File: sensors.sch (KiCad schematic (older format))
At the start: 13 parts, among them U2001 VCNL4040, U2002 LSM9DS1, U2003 74LVC1G332

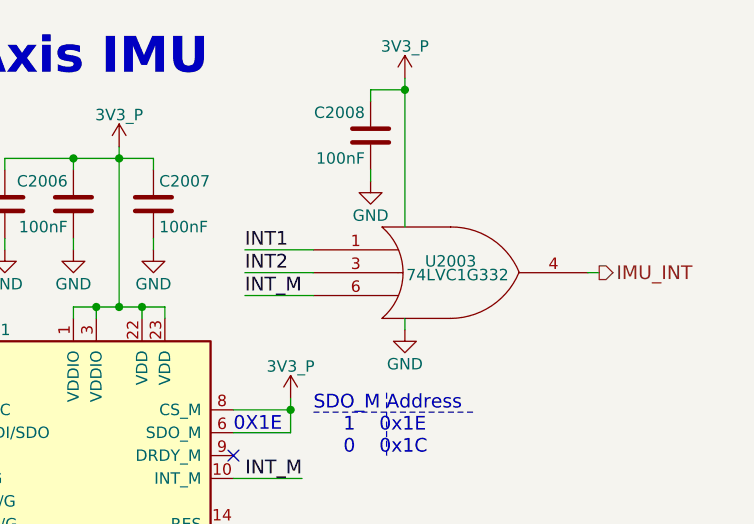
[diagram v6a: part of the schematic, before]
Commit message: Add camera/CSI circuit, include second switch that is part of the audio+camera DPDT for killing both simultaneously, level shifters used for camera's I/O that requires it, footprints for a 1.8V LDO which may be used by DVDD will be included
External DVDD (1.8V LDO) needs to be tested if it's needed (datasheet says an internal DVDD can be used, as is the case with Boundary Devices' OV5640 camera).
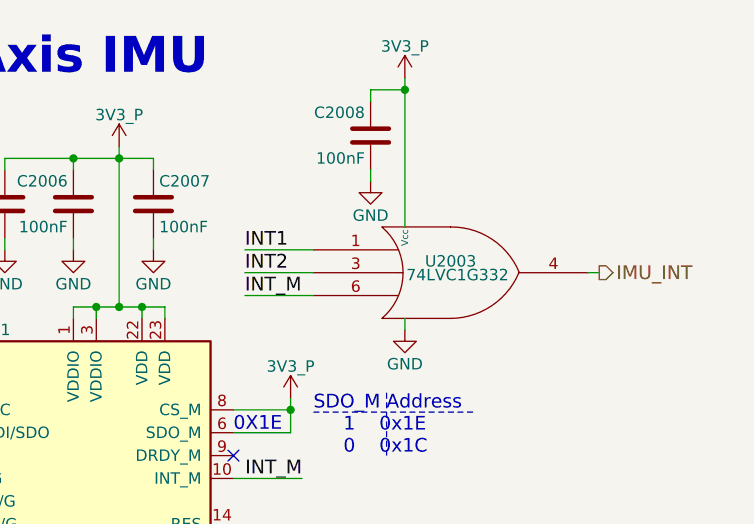
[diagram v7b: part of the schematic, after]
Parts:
- removed U2003: 74LVC1G332, http://www.ti.com/lit/ds/symlink/sn74lvc1g332.pdf, symbol SN74LVC1G332
- added U2003: 74LVC1G332, symbol 74LVC1G332
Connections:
- net 3V3_P: now also U2003.5 (Vcc)
- net GND: now also U2003.2 (GND)
- net IMU_INT: now also U2003.4
- net INT1: now also U2003.1
- net INT2: now also U2003.3
- net INT_M: now also U2003.6
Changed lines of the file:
@@
 $EndComp
 $Comp
-L GND #PWR2005
+L GND #PWR0341
 U 1 1 5B067AE0
 P 4550 3450
-F 0 "#PWR2005" H 4550 3200 50  0001 C CNN
+F 0 "#PWR0341" H 4550 3200 50  0001 C CNN
 F 1 "GND" H 4550 3300 50  0000 C CNN
 F 2 "" H 4550 3450 50  0001 C CNN
@@
 $EndComp
 $Comp
-L GND #PWR2003
+L GND #PWR0342
 U 1 1 5B068781
 P 3800 4100
-F 0 "#PWR2003" H 3800 3850 50  0001 C CNN
+F 0 "#PWR0342" H 3800 3850 50  0001 C CNN
 F 1 "GND" H 3800 3950 50  0000 C CNN
 F 2 "" H 3800 4100 50  0001 C CNN
@@
 $EndComp
 $Comp
-L GND #PWR2002
+L GND #PWR0343
 U 1 1 5B068863
 P 3600 2650
-F 0 "#PWR2002" H 3600 2400 50  0001 C CNN
+F 0 "#PWR0343" H 3600 2400 50  0001 C CNN
 F 1 "GND" H 3600 2500 50  0000 C CNN
 F 2 "" H 3600 2650 50  0001 C CNN
@@
 $EndComp
 $Comp
-L 3V3_P #PWR2004
+L 3V3_P #PWR0344
 U 1 1 5B0689D2
 P 4550 2200
-F 0 "#PWR2004" H 4550 2050 50  0001 C CNN
+F 0 "#PWR0344" H 4550 2050 50  0001 C CNN
 F 1 "3V3_P" H 4550 2350 50  0000 C CNN
 F 2 "" H 4550 2200 50  0001 C CNN
@@
 $EndComp
 $Comp
-L 3V3_P #PWR2001
+L 3V3_P #PWR0345
 U 1 1 5B069B9B
 P 2600 3150
-F 0 "#PWR2001" H 2600 3000 50  0001 C CNN
+F 0 "#PWR0345" H 2600 3000 50  0001 C CNN
 F 1 "3V3_P" H 2600 3290 50  0000 C CNN
 F 2 "" H 2600 3150 50  0001 C CNN
@@
 $EndComp
 $Comp
-L PWR_FLAG #FLG2001
+L PWR_FLAG #FLG0346
 U 1 1 5B13CB3F
 P 3800 2200
-F 0 "#FLG2001" H 3800 2275 50  0001 C CNN
+F 0 "#FLG0346" H 3800 2275 50  0001 C CNN
 F 1 "PWR_FLAG" H 3800 2350 50  0000 C CNN
 F 2 "" H 3800 2200 50  0001 C CNN
@@
 $EndComp
 $Comp
-L GND #PWR2008
+L GND #PWR0347
 U 1 1 5B15906B
 P 8200 4450
-F 0 "#PWR2008" H 8200 4200 50  0001 C CNN
+F 0 "#PWR0347" H 8200 4200 50  0001 C CNN
 F 1 "GND" H 8200 4300 50  0000 C CNN
 F 2 "" H 8200 4450 50  0001 C CNN
@@
 $EndComp
 $Comp
-L 3V3_P #PWR2010
+L 3V3_P #PWR0348
 U 1 1 5B15B71F
 P 8500 1800
-F 0 "#PWR2010" H 8500 1650 50  0001 C CNN
+F 0 "#PWR0348" H 8500 1650 50  0001 C CNN
 F 1 "3V3_P" H 8500 1940 50  0000 C CNN
 F 2 "" H 8500 1800 50  0001 C CNN
@@
 $EndComp
 $Comp
-L GND #PWR2011
+L GND #PWR0349
 U 1 1 5B15B942
 P 8650 2250
-F 0 "#PWR2011" H 8650 2000 50  0001 C CNN
+F 0 "#PWR0349" H 8650 2000 50  0001 C CNN
 F 1 "GND" H 8650 2100 50  0000 C CNN
 F 2 "" H 8650 2250 50  0001 C CNN
@@
 $EndComp
 $Comp
-L GND #PWR2009
+L GND #PWR0350
 U 1 1 5B15B987
 P 8300 2250
-F 0 "#PWR2009" H 8300 2000 50  0001 C CNN
+F 0 "#PWR0350" H 8300 2000 50  0001 C CNN
 F 1 "GND" H 8300 2100 50  0000 C CNN
 F 2 "" H 8300 2250 50  0001 C CNN
@@
 $EndComp
 $Comp
-L GND #PWR2007
+L GND #PWR0351
 U 1 1 5B15BC52
 P 8000 2250
-F 0 "#PWR2007" H 8000 2000 50  0001 C CNN
+F 0 "#PWR0351" H 8000 2000 50  0001 C CNN
 F 1 "GND" H 8000 2100 50  0000 C CNN
 F 2 "" H 8000 2250 50  0001 C CNN
@@
 	-1   0    0    -1
 $EndComp
-$Comp
-L SN74LVC1G332 U2003
-U 1 1 5B168FC1
-P 9950 2350
-F 0 "U2003" H 9950 2400 50  0000 C CNN
-F 1 "74LVC1G332" H 9980 2340 50  0000 C CNN
-F 2 "http://www.ti.com/lit/ds/symlink/sn74lvc1g332.pdf" H 9950 2350 50  0001 C CNN
-F 3 "" H 9950 2350 50  0001 C CNN
-F 4 "Texas Instruments" H 9950 2350 60  0001 C CNN "MFG Name"
-F 5 "SN74LVC1G332DCKR" H 9950 2350 60  0001 C CNN "MFG Part Num"
-F 6 "SN74LVC1G332DCKR" H 9950 2350 60  0001 C CNN "Distrib PN"
-F 7 "https://store.ti.com/SN74LVC1G332DCKR.aspx?HQS=corp-tistore-null-storeinv-invf-store-octopart-wwe" H 9950 2350 60  0001 C CNN "Distrib Link"
-F 8 "-" H 9950 2350 60  0001 C CNN "Tolerance"
-F 9 "https://www.digikey.com/products/en/integrated-circuits-ics/logic-gates-and-inverters/705?FV=ffe002c1&quantity=&ColumnSort=1000011&page=1&k=1G332&pageSize=500" H 9950 2350 60  0001 C CNN "Others"
-	1    9950 2350
-	1    0    0    -1
-$EndComp
 Text Label 9050 2450 0    60   ~ 0
 INT_M
@@
 INT_M
 $Comp
-L 3V3_P #PWR2006
+L 3V3_P #PWR0352
 U 1 1 5B176622
 P 6900 3200
-F 0 "#PWR2006" H 6900 3050 50  0001 C CNN
+F 0 "#PWR0352" H 6900 3050 50  0001 C CNN
 F 1 "3V3_P" H 6900 3340 50  0000 C CNN
 F 2 "" H 6900 3200 50  0001 C CNN
@@
 $EndComp
 $Comp
-L 3V3_P #PWR2012
+L 3V3_P #PWR0353
 U 1 1 5B1766DE
 P 9250 2900
-F 0 "#PWR2012" H 9250 2750 50  0001 C CNN
+F 0 "#PWR0353" H 9250 2750 50  0001 C CNN
 F 1 "3V3_P" H 9250 3040 50  0000 C CNN
 F 2 "" H 9250 2900 50  0001 C CNN
@@
 	8000 2200 8000 2250
 $Comp
-L GND #PWR2015
+L GND #PWR0354
 U 1 1 5B0CAE93
 P 9750 2600
-F 0 "#PWR2015" H 9750 2350 50  0001 C CNN
+F 0 "#PWR0354" H 9750 2350 50  0001 C CNN
 F 1 "GND" H 9750 2450 50  0000 C CNN
 F 2 "" H 9750 2600 50  0001 C CNN
@@
 	9750 2550 9750 2600
 $Comp
-L 3V3_P #PWR2014
+L 3V3_P #PWR0355
 U 1 1 5B0CB162
 P 9750 1500
-F 0 "#PWR2014" H 9750 1350 50  0001 C CNN
+F 0 "#PWR0355" H 9750 1350 50  0001 C CNN
 F 1 "3V3_P" H 9750 1640 50  0000 C CNN
 F 2 "" H 9750 1500 50  0001 C CNN
@@
 $EndComp
 $Comp
-L GND #PWR2013
+L GND #PWR0356
 U 1 1 5B0EBDA7
 P 9600 1950
-F 0 "#PWR2013" H 9600 1700 50  0001 C CNN
+F 0 "#PWR0356" H 9600 1700 50  0001 C CNN
 F 1 "GND" H 9600 1800 50  0000 C CNN
 F 2 "" H 9600 1950 50  0001 C CNN
@@
 Wire Wire Line
 	9600 1900 9600 1950
+$Comp
+L 74LVC1G332 U2003
+U 1 1 5B38F34D
+P 9950 2350
+F 0 "U2003" H 9950 2400 50  0000 C CNN
+F 1 "74LVC1G332" H 9980 2340 50  0000 C CNN
+F 2 "" H 9950 2350 50  0001 C CNN
+F 3 "http://www.ti.com/lit/ds/symlink/sn74lvc1g332.pdf" H 9950 2350 50  0001 C CNN
+F 4 "Texas Instruments" H 9950 2350 60  0001 C CNN "MFG Name"
+F 5 "SN74LVC1G332DCKR" H 9950 2350 60  0001 C CNN "MFG Part Num"
+F 6 "SN74LVC1G332DCKR" H 9950 2350 60  0001 C CNN "Distrib PN"
+F 7 "https://store.ti.com/SN74LVC1G332DCKR.aspx?HQS=corp-tistore-null-storeinv-invf-store-octopart-wwe" H 9950 2350 60  0001 C CNN "Distrib Link"
+F 8 "-" H 9950 2350 60  0001 C CNN "Tolerance"
+F 9 "https://www.digikey.com/products/en/integrated-circuits-ics/logic-gates-and-inverters/705?FV=ffe002c1&quantity=&ColumnSort=1000011&page=1&k=1G332&pageSize=500" H 9950 2350 60  0001 C CNN "Others"
+	1    9950 2350
+	1    0    0    -1
+$EndComp
 $EndSCHEMATC

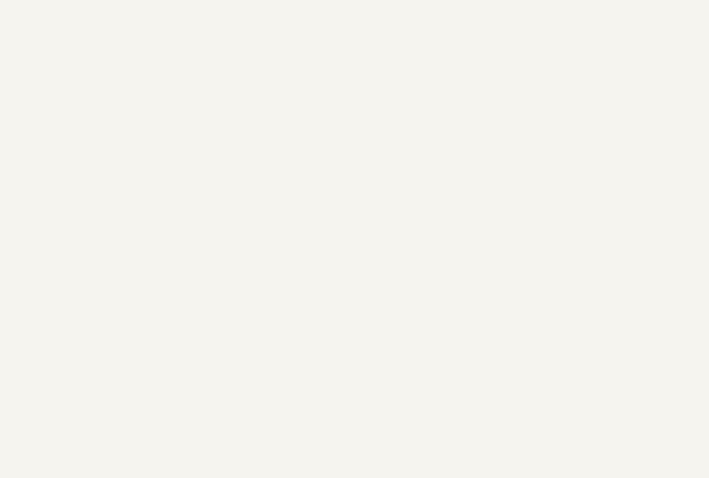
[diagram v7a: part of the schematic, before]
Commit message: added footprints for switches and phone jack new wiring of DPDT switches for HKS purposes
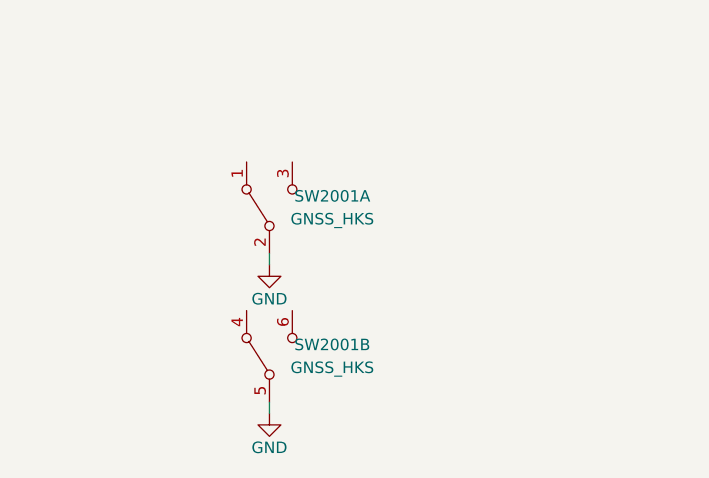
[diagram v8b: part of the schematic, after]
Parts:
- added SW2001: GNSS_HKS, dvk-mx8m-bsb:Switch_CK_DPDT_JS202011JAQN, symbol SW_DPDT_x2
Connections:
- net GND: now also SW2001.2 (B), SW2001.5 (B)
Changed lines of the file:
@@
 $Bitmap
 Pos 7500 5950
-Scale 1.000000
+Scale 1,000000
 Data
 89 50 4E 47 0D 0A 1A 0A 00 00 00 0D 49 48 44 52 00 00 03 77 00 00 01 45 08 02 00 00 00 C0 7C 83
@@
 $Bitmap
 Pos 10100 5950
-Scale 1.000000
+Scale 1,000000
 Data
 89 50 4E 47 0D 0A 1A 0A 00 00 00 0D 49 48 44 52 00 00 02 A2 00 00 01 63 08 02 00 00 00 69 3F FE
@@
 	1    0    0    -1
 $EndComp
+$Comp
+L SW_DPDT_x2 SW2001
+U 1 1 5B1273A9
+P 2700 5800
+F 0 "SW2001" V 2750 5525 50  0000 C CNN
+F 1 "GNSS_HKS" V 2650 5525 50  0000 C CNN
+F 2 "dvk-mx8m-bsb:Switch_CK_DPDT_JS202011JAQN" H 2700 5800 50  0001 C CNN
+F 3 "https://www.ckswitches.com/media/1422/js.pdf" H 2700 5800 50  0001 C CNN
+F 4 "C&K" V 2700 5800 60  0001 C CNN "MFG Name"
+F 5 "JS202011JAQN" V 2700 5800 60  0001 C CNN "MFG Part Num"
+F 6 "CKN10722CT-ND" V 2700 5800 60  0001 C CNN "Distrib PN"
+F 7 "https://www.digikey.de/product-detail/de/c-k/JS202011JAQN/CKN10722CT-ND/6137636" V 2700 5800 60  0001 C CNN "Distrib Link"
+F 8 "-" V 2700 5800 60  0001 C CNN "Tolerance"
+F 9 "https://www.digikey.com/products/en/switches/slide-switches/213?FV=2080004%2Cffe000d5%2C1140003%2C1140160%2C1f140000&quantity=&ColumnSort=1000011&page=1&pageSize=500" V 2700 5800 60  0001 C CNN "Others"
+	1    2700 5800
+	0    -1   -1   0
+$EndComp
+$Comp
+L SW_DPDT_x2 SW2001
+U 2 1 5B12744E
+P 2700 6450
+F 0 "SW2001" V 2750 6175 50  0000 C CNN
+F 1 "GNSS_HKS" V 2650 6175 50  0000 C CNN
+F 2 "dvk-mx8m-bsb:Switch_CK_DPDT_JS202011JAQN" H 2700 6450 50  0001 C CNN
+F 3 "https://www.ckswitches.com/media/1422/js.pdf" H 2700 6450 50  0001 C CNN
+F 4 "C&K" V 2700 6450 60  0001 C CNN "MFG Name"
+F 5 "JS202011JAQN" V 2700 6450 60  0001 C CNN "MFG Part Num"
+F 6 "CKN10722CT-ND" V 2700 6450 60  0001 C CNN "Distrib PN"
+F 7 "https://www.digikey.de/product-detail/de/c-k/JS202011JAQN/CKN10722CT-ND/6137636" V 2700 6450 60  0001 C CNN "Distrib Link"
+F 8 "-" V 2700 6450 60  0001 C CNN "Tolerance"
+F 9 "https://www.digikey.com/products/en/switches/slide-switches/213?FV=2080004%2Cffe000d5%2C1140003%2C1140160%2C1f140000&quantity=&ColumnSort=1000011&page=1&pageSize=500" V 2700 6450 60  0001 C CNN "Others"
+	2    2700 6450
+	0    -1   -1   0
+$EndComp
+$Comp
+L GND #PWR?
+U 1 1 5B127823
+P 2700 6050
+F 0 "#PWR?" H 2700 5800 50  0001 C CNN
+F 1 "GND" H 2700 5900 50  0000 C CNN
+F 2 "" H 2700 6050 50  0001 C CNN
+F 3 "" H 2700 6050 50  0001 C CNN
+	1    2700 6050
+	1    0    0    -1
+$EndComp
+$Comp
+L GND #PWR?
+U 1 1 5B12790B
+P 2700 6700
+F 0 "#PWR?" H 2700 6450 50  0001 C CNN
+F 1 "GND" H 2700 6550 50  0000 C CNN
+F 2 "" H 2700 6700 50  0001 C CNN
+F 3 "" H 2700 6700 50  0001 C CNN
+	1    2700 6700
+	1    0    0    -1
+$EndComp
+Wire Wire Line
+	2700 6050 2700 6000
+Wire Wire Line
+	2700 6700 2700 6650
 $EndSCHEMATC
